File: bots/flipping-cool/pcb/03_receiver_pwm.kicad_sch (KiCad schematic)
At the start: 2 parts, among them J10 MATEK_ELRS_R24_P6_PWM, J11 R24_P6_VBAT_TELEMETRY_SENSE

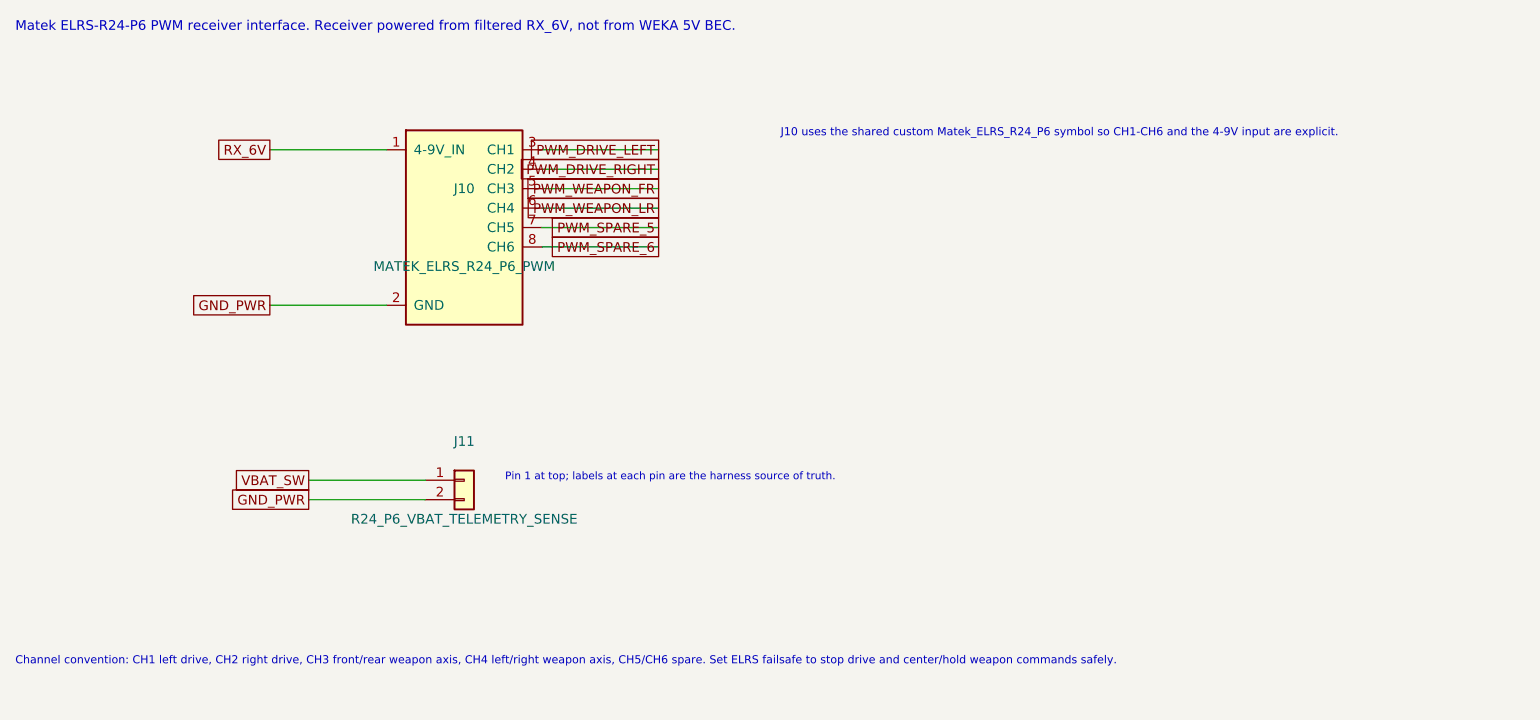
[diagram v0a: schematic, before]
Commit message: Refactor Flipping Cool PCB design to Rev B, updating title, date, and revision details. Integrate ESP32-S3 module and enhance documentation for MCU I/O and debugging features, while maintaining historical context from Rev A.
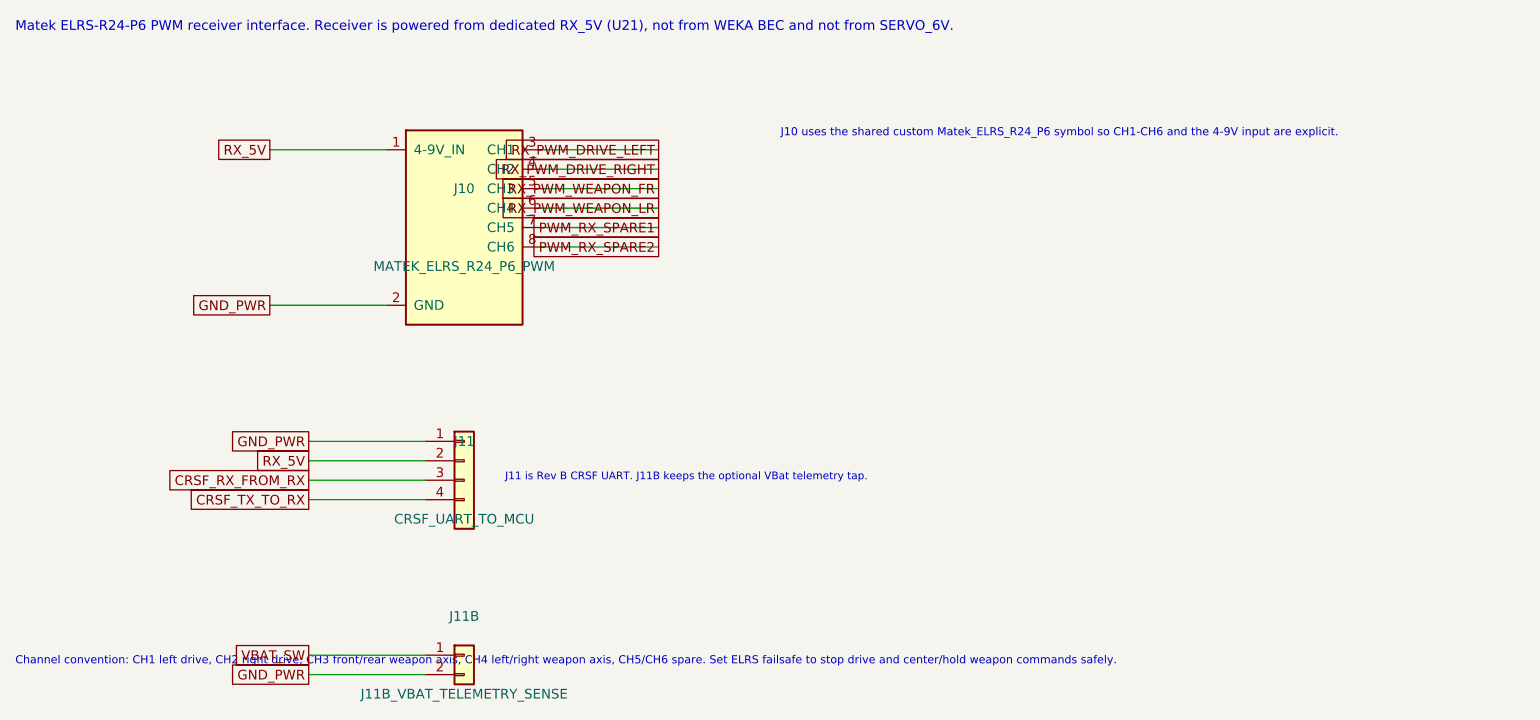
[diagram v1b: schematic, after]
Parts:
- added J11B: J11B_VBAT_TELEMETRY_SENSE, Connector_PinHeader_2.54mm:PinHeader_1x02_P2.54mm_Vertical, symbol Connector_Generic:Conn_01x02
- J11: value R24_P6_VBAT_TELEMETRY_SENSE -> CRSF_UART_TO_MCU; footprint Connector_PinHeader_2.54mm:PinHeader_1x02_P2.54mm_Vertical -> Connector_JST:JST_SH_SM04B-SRSS-TB_1x04-1MP_P1.00mm_Horizontal; symbol Connector_Generic:Conn_01x02 -> Connector_Generic:Conn_01x04
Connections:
- net GND_PWR: now also J11.1 (Pin_1), J11B.2 (Pin_2); no longer J11.2 (Pin_2)
- net VBAT_SW: now also J11B.1 (Pin_1); no longer J11.1 (Pin_1)
- net PWM_DRIVE_LEFT renamed RX_PWM_DRIVE_LEFT
- net PWM_DRIVE_RIGHT renamed RX_PWM_DRIVE_RIGHT
- net PWM_SPARE_5 renamed PWM_RX_SPARE1
- net PWM_SPARE_6 renamed PWM_RX_SPARE2
- net PWM_WEAPON_FR renamed RX_PWM_WEAPON_FR
- net PWM_WEAPON_LR renamed RX_PWM_WEAPON_LR
- net RX_6V renamed RX_5V
- net RX_5V: now also J11.2 (Pin_2)
- new net CRSF_RX_FROM_RX: J11.3 (Pin_3)
- new net CRSF_TX_TO_RX: J11.4 (Pin_4)
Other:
- note added: "J11 is Rev B CRSF UART. J11B keeps the optional VBat telemetry tap."
- note added: "Matek ELRS-R24-P6 PWM receiver interface. Receiver is powered from dedicated RX_5V (U21), not from WEKA BEC and not from SERVO_6V."
- note removed: "Matek ELRS-R24-P6 PWM receiver interface. Receiver powered from filtered RX_6V, not from WEKA 5V BEC."
- note removed: "Pin 1 at top; labels at each pin are the harness source of truth."
- title: Flipping Cool Rev A - Receiver PWM -> Flipping Cool Rev B - Receiver and CRSF
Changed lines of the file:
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@@
-(kicad_sch
-  (version 20250114)
-  (generator "codex")
-  (generator_version "9.0")
-  (paper "A4")
-  (title_block
-    (title "Flipping Cool Rev A - Receiver PWM")
-    (date "2026-05-08")
-    (rev "A")
-    (company "battle_bots_ai")
-  )
-  (text "Matek ELRS-R24-P6 PWM receiver interface. Receiver powered from filtered RX_6V, not from WEKA 5V BEC."
-    (at 15.00 15.00 0)
-    (effects (font (size 1.27 1.27)) (justify left top))
-  )
-  (symbol
-    (lib_id "custom:Matek_ELRS_R24_P6")
-    (at 73.66 41.91 0)
-    (unit 1)
-    (exclude_from_sim no)
-    (in_bom yes)
-    (on_board yes)
-    (dnp no)
-    (property "Reference" "J10"
-      (at 73.66 36.83 0)
-      (effects (font (size 1.27 1.27)))
-    )
-    (property "Value" "MATEK_ELRS_R24_P6_PWM"
-      (at 73.66 46.99 0)
-      (effects (font (size 1.27 1.27)))
-    )
-    (property "Footprint" "Connector_PinHeader_2.54mm:PinHeader_1x08_P2.54mm_Vertical"
-      (at 73.66 41.91 0)
-      (effects (font (size 1.27 1.27)))
-      (hide yes)
-    )
-    (property "Datasheet" "https://www.mateksys.com/?portfolio=elrs-r24-p6"
-      (at 73.66 41.91 0)
-      (effects (font (size 1.27 1.27)))
-      (hide yes)
-    )
-    (property "Description" "Named-pin ELRS receiver interface: 4-9V_IN, GND, CH1-CH6."
-      (at 73.66 41.91 0)
-      (effects (font (size 1.27 1.27)))
-      (hide yes)
-    )
-    (pin "1"
-    )
-    (pin "2"
-    )
-    (pin "3"
-    )
-    (pin "4"
-    )
-    (pin "5"
-    )
-    (pin "6"
-    )
-    (pin "7"
-    )
-    (pin "8"
-    )
-    (instances (project "flipping-cool" (path "/" (reference "J10") (unit 1))))
-  )
-  (wire
-    (pts (xy 63.50 31.75) (xy 48.26 31.75))
-    (stroke (width 0) (type solid))
-  )
-  (global_label "RX_6V" (shape passive)
-    (at 48.26 31.75 180)
-    (effects (font (size 1.27 1.27)) (justify right bottom))
-  )
-  (wire
-    (pts (xy 63.50 52.07) (xy 48.26 52.07))
-    (stroke (width 0) (type solid))
-  )
-  (global_label "GND_PWR" (shape passive)
-    (at 48.26 52.07 180)
-    (effects (font (size 1.27 1.27)) (justify right bottom))
-  )
-  (wire
-    (pts (xy 83.82 31.75) (xy 99.06 31.75))
-    (stroke (width 0) (type solid))
-  )
-  (global_label "PWM_DRIVE_LEFT" (shape passive)
-    (at 99.06 31.75 180)
-    (effects (font (size 1.27 1.27)) (justify right bottom))
-  )
-  (wire
-    (pts (xy 83.82 34.29) (xy 99.06 34.29))
-    (stroke (width 0) (type solid))
-  )
-  (global_label "PWM_DRIVE_RIGHT" (shape passive)
-    (at 99.06 34.29 180)
-    (effects (font (size 1.27 1.27)) (justify right bottom))
-  )
-  (wire
-    (pts (xy 83.82 36.83) (xy 99.06 36.83))
-    (stroke (width 0) (type solid))
-  )
-  (global_label "PWM_WEAPON_FR" (shape passive)
-    (at 99.06 36.83 180)
-    (effects (font (size 1.27 1.27)) (justify right bottom))
-  )
-  (wire
-    (pts (xy 83.82 39.37) (xy 99.06 39.37))
-    (stroke (width 0) (type solid))
-  )
-  (global_label "PWM_WEAPON_LR" (shape passive)
-    (at 99.06 39.37 180)
-    (effects (font (size 1.27 1.27)) (justify right bottom))
-  )
-  (wire
-    (pts (xy 83.82 41.91) (xy 99.06 41.91))
-    (stroke (width 0) (type solid))
-  )
-  (global_label "PWM_SPARE_5" (shape passive)
-    (at 99.06 41.91 180)
-    (effects (font (size 1.27 1.27)) (justify right bottom))
-  )
-  (wire
-    (pts (xy 83.82 44.45) (xy 99.06 44.45))
-    (stroke (width 0) (type solid))
-  )
-  (global_label "PWM_SPARE_6" (shape passive)
-    (at 99.06 44.45 180)
-    (effects (font (size 1.27 1.27)) (justify right bottom))
-  )
-  (text "J10 uses the shared custom Matek_ELRS_R24_P6 symbol so CH1-CH6 and the 4-9V input are explicit."
-    (at 115.00 29.00 0)
-    (effects (font (size 1.05 1.05)) (justify left top))
-  )
-  (symbol
-    (lib_id "Connector_Generic:Conn_01x02")
-    (at 73.66 74.93 0)
-    (unit 1)
-    (exclude_from_sim no)
-    (in_bom yes)
-    (on_board yes)
-    (dnp no)
-    (property "Reference" "J11"
-      (at 73.66 69.85 0)
-      (effects (font (size 1.27 1.27)))
-    )
-    (property "Value" "R24_P6_VBAT_TELEMETRY_SENSE"
-      (at 73.66 80.01 0)
-      (effects (font (size 1.27 1.27)))
-    )
-    (property "Footprint" "Connector_PinHeader_2.54mm:PinHeader_1x02_P2.54mm_Vertical"
-      (at 73.66 74.93 0)
-      (effects (font (size 1.27 1.27)))
-      (hide yes)
-    )
-    (property "Datasheet" "https://www.mateksys.com/?portfolio=elrs-r24-p6"
-      (at 73.66 74.93 0)
-      (effects (font (size 1.27 1.27)))
-      (hide yes)
-    )
-    (property "Description" "Optional VBAT sense to R24-P6 VBat pad, 34V max. Sense only; not receiver power."
-      (at 73.66 74.93 0)
-      (effects (font (size 1.27 1.27)))
-      (hide yes)
-    )
-    (pin "1"
-    )
-    (pin "2"
-    )
-    (instances (project "flipping-cool" (path "/" (reference "J11") (unit 1))))
-  )
-  (wire
-    (pts (xy 68.58 74.93) (xy 53.34 74.93))
-    (stroke (width 0) (type solid))
-  )
-  (global_label "VBAT_SW" (shape passive)
-    (at 53.34 74.93 180)
-    (effects (font (size 1.27 1.27)) (justify right bottom))
-  )
-  (wire
-    (pts (xy 68.58 77.47) (xy 53.34 77.47))
-    (stroke (width 0) (type solid))
-  )
-  (global_label "GND_PWR" (shape passive)
-    (at 53.34 77.47 180)
-    (effects (font (size 1.27 1.27)) (justify right bottom))
-  )
-  (text "Pin 1 at top; labels at each pin are the harness source of truth."
-    (at 79.00 74.00 0)
-    (effects (font (size 1.00 1.00)) (justify left top))
-  )
-  (text "Channel convention: CH1 left drive, CH2 right drive, CH3 front/rear weapon axis, CH4 left/right weapon axis, CH5/CH6 spare. Set ELRS failsafe to stop drive and center/hold weapon commands safely."
-    (at 15.00 98.00 0)
-    (effects (font (size 1.05 1.05)) (justify left top))
-  )
-  (sheet_instances
-    (path "/ec305eb4-293a-58dd-b3b3-f8cf96ed735b/" (page "5"))
-  )
-)

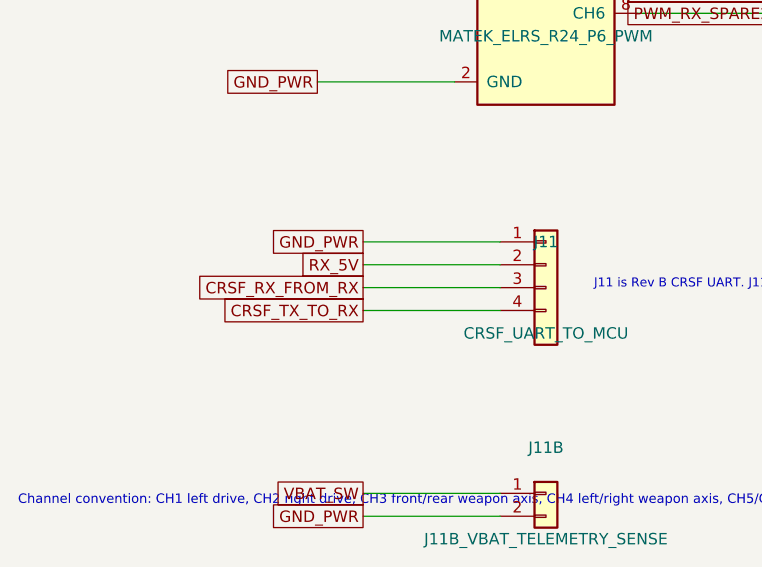
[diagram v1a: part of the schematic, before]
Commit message: Remove obsolete Flipping Cool Rev B project plan file and update schematic files to reflect the latest design changes, including integration of the ESP32-S3 module and enhancements to power management and control authority. Ensure all documentation is aligned with the current PCB design and architecture.
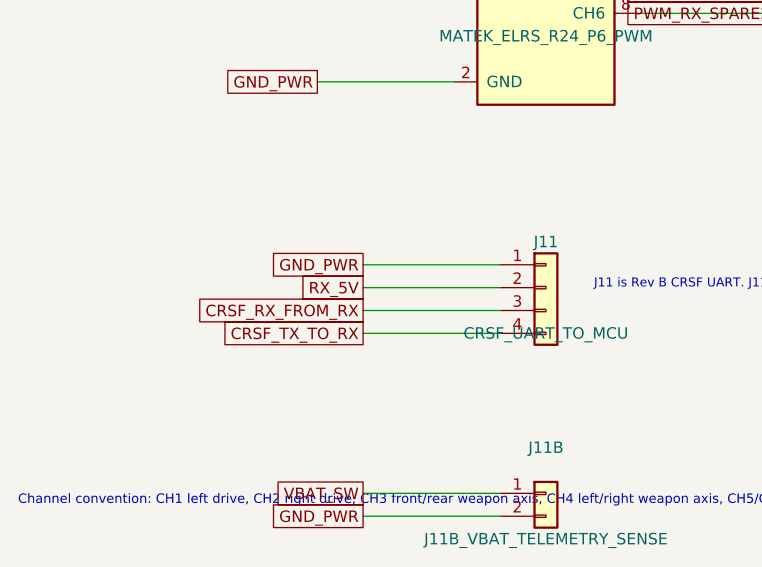
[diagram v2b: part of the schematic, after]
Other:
- moved on the sheet: J11
